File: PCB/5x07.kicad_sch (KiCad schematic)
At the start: 28 parts, among them J1 AVR-ISP-6, J2 AudioJack3_Ground, SW1 SW_Push, U1 ATmega32U4-A, U2 PRTR5V0U2X, Y1 16MHz

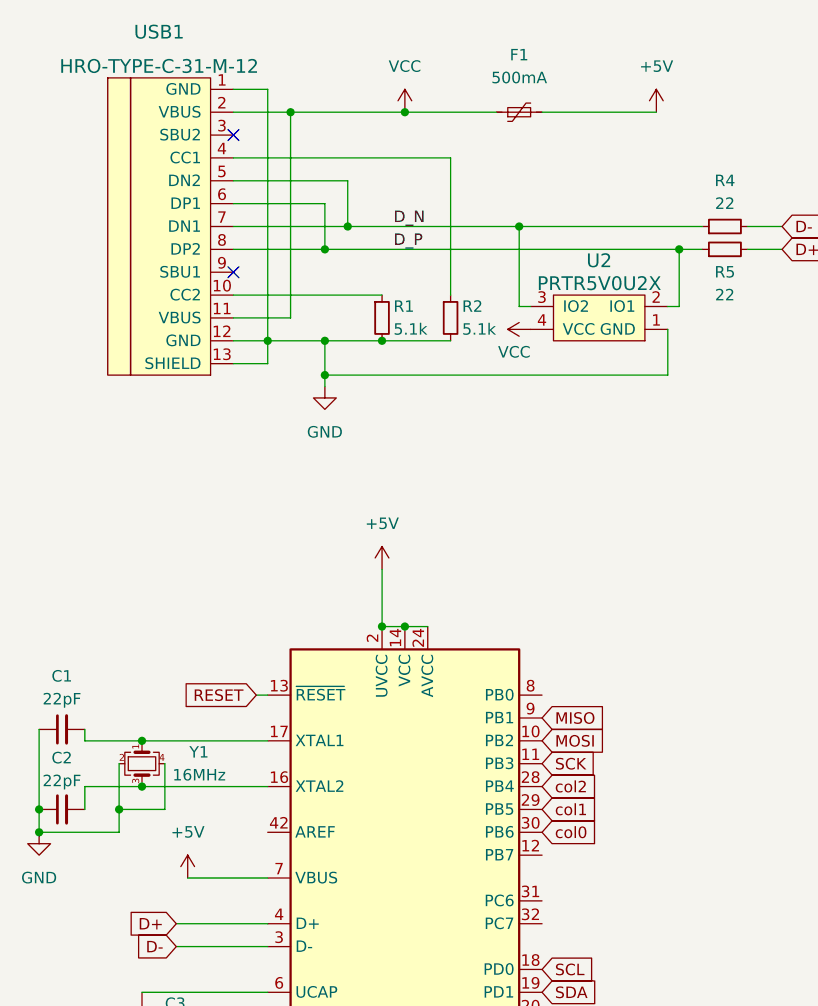
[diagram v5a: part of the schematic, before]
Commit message: added vbus detection compatibility
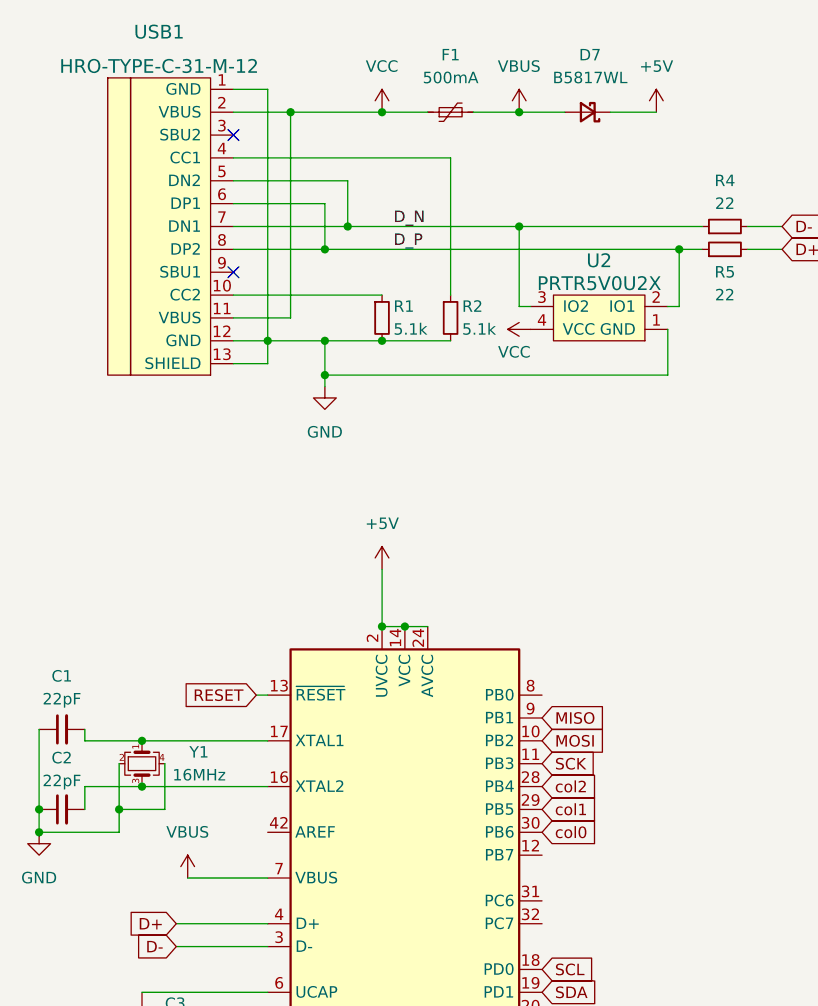
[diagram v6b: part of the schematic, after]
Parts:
- added D7: B5817WL, Diode_SMD:D_SOD-123F, symbol Device:D_Schottky_Small
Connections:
- net +5V: now also D7.1 (K); no longer F1.2, U1.7 (VBUS)
- new net VBUS: D7.2 (A), F1.2, U1.7 (VBUS)
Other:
- moved on the sheet: F1
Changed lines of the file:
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@@
   (junction (at 63.5 63.5) (diameter 0) (color 0 0 0 0)
   )
-  (junction (at 66.04 38.1) (diameter 0) (color 0 0 0 0)
-  )
   (junction (at 57.15 53.34) (diameter 0) (color 0 0 0 0)
   )
@@
   (junction (at 125.73 175.26) (diameter 0) (color 0 0 0 0)
   )
+  (junction (at 78.74 38.1) (diameter 0) (color 0 0 0 0)
+  )
   (junction (at 78.74 50.8) (diameter 0) (color 0 0 0 0)
   )
@@
   )
   (junction (at 63.5 186.69) (diameter 0) (color 0 0 0 0)
+  )
+  (junction (at 63.5 38.1) (diameter 0) (color 0 0 0 0)
   )
   (no_connect (at 46.99 40.64))
@@
     (stroke (width 0) (type default) (color 0 0 0 0))
   )
-  (wire (pts (xy 66.04 38.1) (xy 76.2 38.1))
-    (stroke (width 0) (type default) (color 0 0 0 0))
-  )
   (wire (pts (xy 46.99 53.34) (xy 57.15 53.34))
     (stroke (width 0) (type default) (color 0 0 0 0))
@@
     (stroke (width 0) (type default) (color 0 0 0 0))
   )
+  (wire (pts (xy 63.5 38.1) (xy 68.58 38.1))
+    (stroke (width 0) (type default) (color 0 0 0 0))
+  )
   (wire (pts (xy 57.15 63.5) (xy 63.5 63.5))
     (stroke (width 0) (type default) (color 0 0 0 0))
@@
     (stroke (width 0) (type default) (color 0 0 0 0))
   )
+  (wire (pts (xy 88.9 38.1) (xy 93.98 38.1))
+    (stroke (width 0) (type default) (color 0 0 0 0))
+  )
   (wire (pts (xy 115.57 180.34) (xy 125.73 180.34))
     (stroke (width 0) (type default) (color 0 0 0 0))
@@
     (stroke (width 0) (type default) (color 0 0 0 0))
   )
-  (wire (pts (xy 53.34 38.1) (xy 66.04 38.1))
+  (wire (pts (xy 53.34 38.1) (xy 63.5 38.1))
     (stroke (width 0) (type default) (color 0 0 0 0))
   )
@@
     (stroke (width 0) (type default) (color 0 0 0 0))
   )
+  (wire (pts (xy 78.74 38.1) (xy 83.82 38.1))
+    (stroke (width 0) (type default) (color 0 0 0 0))
+  )
   (wire (pts (xy 104.14 53.34) (xy 107.95 53.34))
     (stroke (width 0) (type default) (color 0 0 0 0))
@@
     (stroke (width 0) (type default) (color 0 0 0 0))
   )
-  (wire (pts (xy 81.28 38.1) (xy 93.98 38.1))
+  (wire (pts (xy 73.66 38.1) (xy 78.74 38.1))
     (stroke (width 0) (type default) (color 0 0 0 0))
   )
@@
     )
     (property "Datasheet" "" (id 3) (at 80.01 62.23 0)
+      (effects (font (size 1.27 1.27)) hide)
+    )
+    (pin "1")
+  )
+  (symbol (lib_id "power:VBUS") (at 78.74 38.1 0) (unit 1)
+    (in_bom yes) (on_board yes) (fields_autoplaced)
+    (property "Reference" "#PWR?" (id 0) (at 78.74 41.91 0)
+      (effects (font (size 1.27 1.27)) hide)
+    )
+    (property "Value" "VBUS" (id 1) (at 78.74 33.02 0))
+    (property "Footprint" "" (id 2) (at 78.74 38.1 0)
+      (effects (font (size 1.27 1.27)) hide)
+    )
+    (property "Datasheet" "" (id 3) (at 78.74 38.1 0)
       (effects (font (size 1.27 1.27)) hide)
     )
@@
     )
     (property "Datasheet" "" (id 3) (at 55.88 186.69 0)
+      (effects (font (size 1.27 1.27)) hide)
+    )
+    (pin "1")
+  )
+  (symbol (lib_id "power:VBUS") (at 41.91 123.19 0) (unit 1)
+    (in_bom yes) (on_board yes) (fields_autoplaced)
+    (property "Reference" "#PWR?" (id 0) (at 41.91 127 0)
+      (effects (font (size 1.27 1.27)) hide)
+    )
+    (property "Value" "VBUS" (id 1) (at 41.91 118.11 0))
+    (property "Footprint" "" (id 2) (at 41.91 123.19 0)
+      (effects (font (size 1.27 1.27)) hide)
+    )
+    (property "Datasheet" "" (id 3) (at 41.91 123.19 0)
       (effects (font (size 1.27 1.27)) hide)
     )
@@
     (pin "2")
   )
-  (symbol (lib_id "power:VCC") (at 66.04 38.1 0) (unit 1)
-    (in_bom yes) (on_board yes) (fields_autoplaced)
-    (property "Reference" "#PWR0105" (id 0) (at 66.04 41.91 0)
-      (effects (font (size 1.27 1.27)) hide)
-    )
-    (property "Value" "VCC" (id 1) (at 66.04 33.02 0))
-    (property "Footprint" "" (id 2) (at 66.04 38.1 0)
-      (effects (font (size 1.27 1.27)) hide)
-    )
-    (property "Datasheet" "" (id 3) (at 66.04 38.1 0)
+  (symbol (lib_id "power:VCC") (at 63.5 38.1 0) (unit 1)
+    (in_bom yes) (on_board yes) (fields_autoplaced)
+    (property "Reference" "#PWR0105" (id 0) (at 63.5 41.91 0)
+      (effects (font (size 1.27 1.27)) hide)
+    )
+    (property "Value" "VCC" (id 1) (at 63.5 33.02 0))
+    (property "Footprint" "" (id 2) (at 63.5 38.1 0)
+      (effects (font (size 1.27 1.27)) hide)
+    )
+    (property "Datasheet" "" (id 3) (at 63.5 38.1 0)
       (effects (font (size 1.27 1.27)) hide)
     )
@@
     (pin "1")
     (pin "2")
-  )
-  (symbol (lib_id "power:+5V") (at 41.91 123.19 0) (unit 1)
-    (in_bom yes) (on_board yes) (fields_autoplaced)
-    (property "Reference" "#PWR?" (id 0) (at 41.91 127 0)
-      (effects (font (size 1.27 1.27)) hide)
-    )
-    (property "Value" "+5V" (id 1) (at 41.91 118.11 0))
-    (property "Footprint" "" (id 2) (at 41.91 123.19 0)
-      (effects (font (size 1.27 1.27)) hide)
-    )
-    (property "Datasheet" "" (id 3) (at 41.91 123.19 0)
-      (effects (font (size 1.27 1.27)) hide)
-    )
-    (pin "1")
   )
   (symbol (lib_id "power:+5V") (at 93.98 38.1 0) (unit 1)
@@
     (pin "1")
   )
-  (symbol (lib_id "Device:Polyfuse_Small") (at 78.74 38.1 90) (unit 1)
-    (in_bom yes) (on_board yes) (fields_autoplaced)
-    (property "Reference" "F1" (id 0) (at 78.74 31.75 90))
-    (property "Value" "500mA" (id 1) (at 78.74 34.29 90))
-    (property "Footprint" "Fuse:Fuse_1206_3216Metric_Pad1.42x1.75mm_HandSolder" (id 2) (at 83.82 36.83 0)
-      (effects (font (size 1.27 1.27)) (justify left) hide)
-    )
-    (property "Datasheet" "~" (id 3) (at 78.74 38.1 0)
+  (symbol (lib_id "Device:Polyfuse_Small") (at 71.12 38.1 90) (unit 1)
+    (in_bom yes) (on_board yes) (fields_autoplaced)
+    (property "Reference" "F1" (id 0) (at 71.12 31.75 90))
+    (property "Value" "500mA" (id 1) (at 71.12 34.29 90))
+    (property "Footprint" "Fuse:Fuse_1206_3216Metric_Pad1.42x1.75mm_HandSolder" (id 2) (at 76.2 36.83 0)
+      (effects (font (size 1.27 1.27)) (justify left) hide)
+    )
+    (property "Datasheet" "~" (id 3) (at 71.12 38.1 0)
       (effects (font (size 1.27 1.27)) hide)
     )
@@
     (pin "4")
   )
+  (symbol (lib_id "Device:D_Schottky_Small") (at 86.36 38.1 180) (unit 1)
+    (in_bom yes) (on_board yes) (fields_autoplaced)
+    (property "Reference" "D7" (id 0) (at 86.614 31.75 0))
+    (property "Value" "B5817WL" (id 1) (at 86.614 34.29 0))
+    (property "Footprint" "Diode_SMD:D_SOD-123F" (id 2) (at 86.36 38.1 90)
+      (effects (font (size 1.27 1.27)) hide)
+    )
+    (property "Datasheet" "~" (id 3) (at 86.36 38.1 90)
+      (effects (font (size 1.27 1.27)) hide)
+    )
+    (pin "1")
+    (pin "2")
+  )
   (symbol (lib_id "Device:R_Small") (at 71.12 60.96 0) (unit 1)
     (in_bom yes) (on_board yes)
@@
       (reference "#PWR0119") (unit 1) (value "GND") (footprint "")
     )
-    (path "/98f489ed-2157-4835-a16c-9b0464a0bb90"
-      (reference "#PWR?") (unit 1) (value "+5V") (footprint "")
+    (path "/1744ee6e-12a9-40a5-9c15-d14a80551938"
+      (reference "#PWR?") (unit 1) (value "VBUS") (footprint "")
+    )
+    (path "/39ebe98d-e5dc-4b0f-950b-000b98bf51e8"
+      (reference "#PWR?") (unit 1) (value "VBUS") (footprint "")
     )
     (path "/a3d05fbb-612d-426a-9aec-e5dec820a7f7"
@@
       (reference "D6") (unit 1) (value "D_Small") (footprint "assets:D_SOD-123-Reversible")
     )
+    (path "/ed0b7c31-165e-4918-9fa1-51794dfb7d46"
+      (reference "D7") (unit 1) (value "B5817WL") (footprint "Diode_SMD:D_SOD-123F")
+    )
     (path "/4787577f-7d8a-45a2-be7c-203d64397828/bc06fd3c-fdee-456d-a7b7-262148242cc2"
